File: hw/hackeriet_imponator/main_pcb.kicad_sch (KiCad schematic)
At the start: 10 parts, among them J1 AVR-ISP-6, J2 Battery connector, U1 ATmega328PB-A

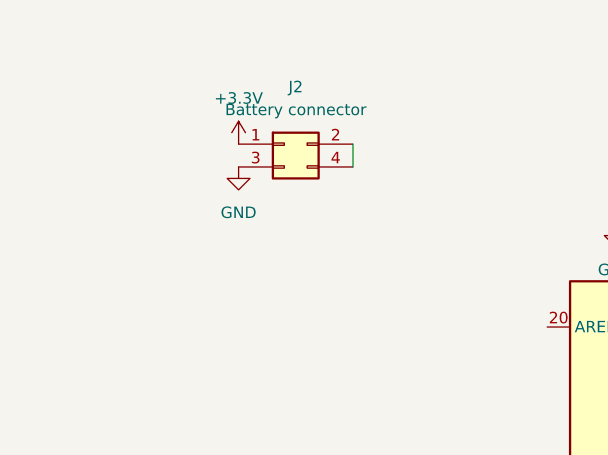
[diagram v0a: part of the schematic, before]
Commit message: Added Batttery holders. Some general routing
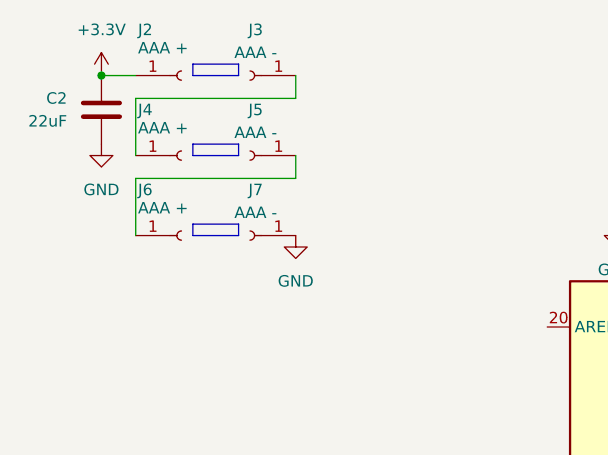
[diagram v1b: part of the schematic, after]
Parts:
- removed J2: Battery connector, imponator_footprint_lib:BAT_1022, symbol Connector_Generic:Conn_02x02_Odd_Even
- added C2: 22uF, Capacitor_SMD:C_0603_1608Metric_Pad1.08x0.95mm_HandSolder, symbol Device:C
- added J2, J4, J6: AAA +, imponator_footprint_lib:BAT_597, symbol Connector:Conn_01x01_Socket
- added J3, J5, J7: AAA -, imponator_footprint_lib:BAT_591, symbol Connector:Conn_01x01_Socket
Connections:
- net +3.3V: now also C2.2, J2.1 (Pin_1)
- net GND: now also C2.1, J7.1 (Pin_1)
- new net: J3.1 (Pin_1), J4.1 (Pin_1)
- new net: J5.1 (Pin_1), J6.1 (Pin_1)

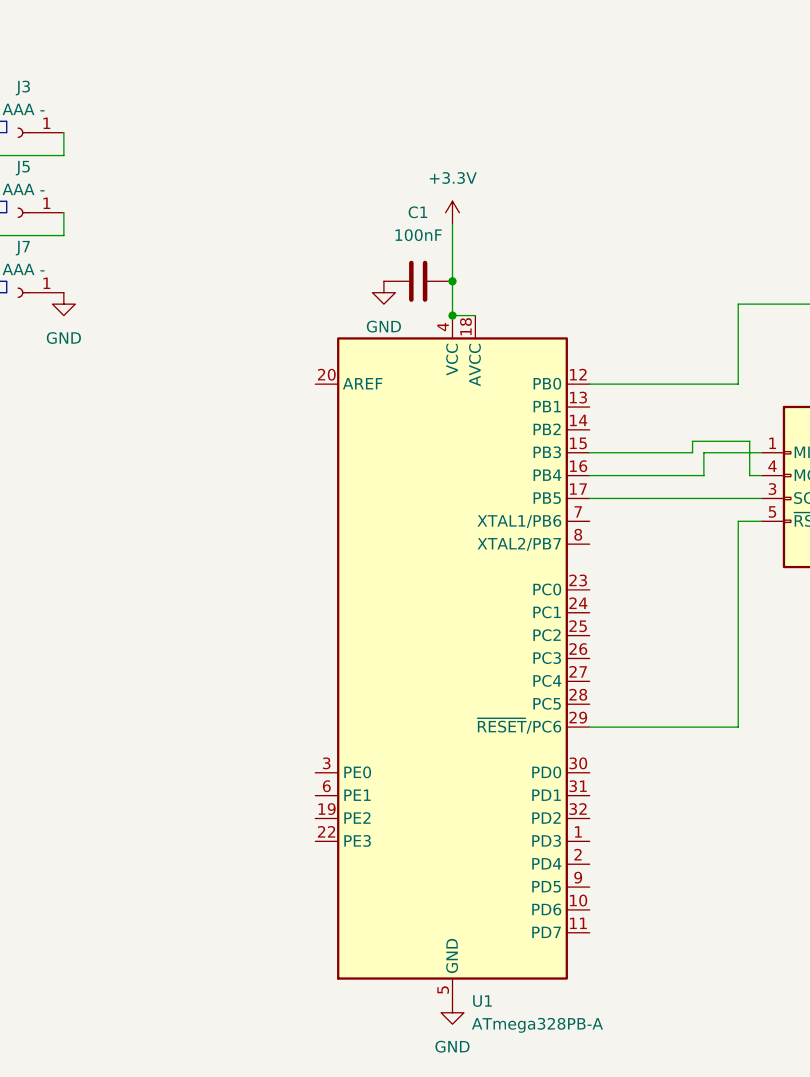
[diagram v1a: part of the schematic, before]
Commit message: Started changing out ATmega328P with ATmega32URC because the latter got built-in USB driver, making the design easier, if a bit more expensive
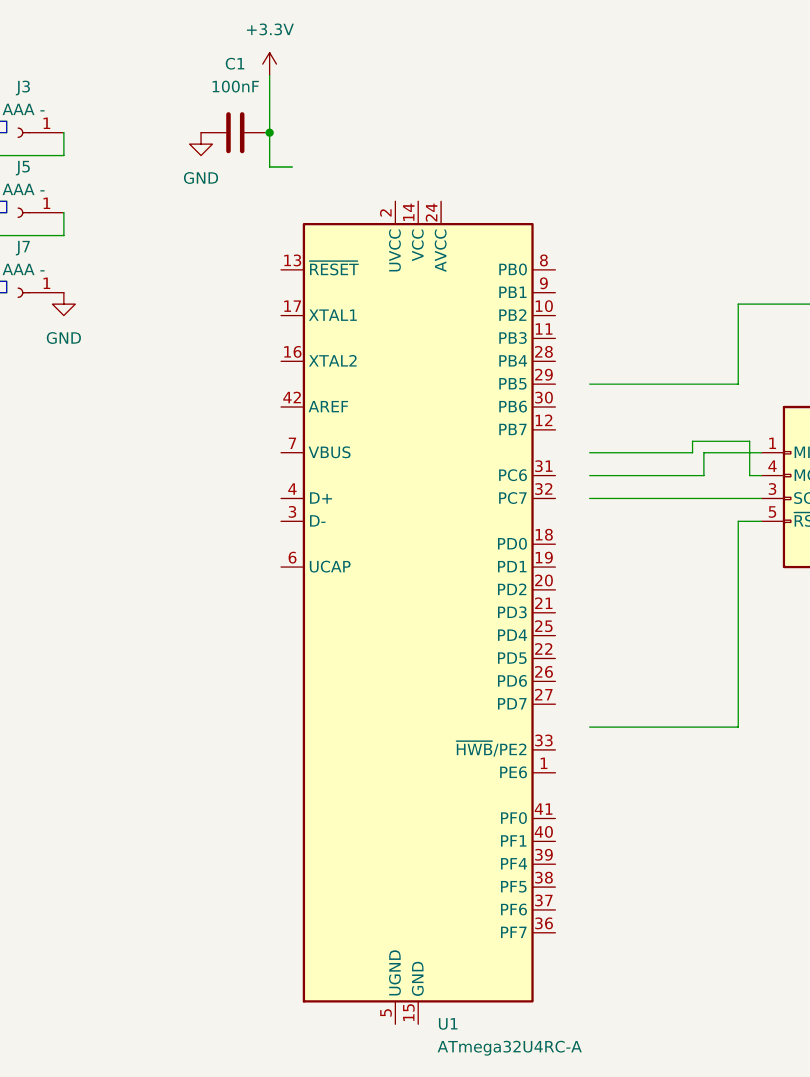
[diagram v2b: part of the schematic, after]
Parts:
- removed U1: ATmega328PB-A, Package_QFP:TQFP-32_7x7mm_P0.8mm, symbol MCU_Microchip_ATmega:ATmega328PB-A
- added U1: ATmega32U4RC-A, Package_QFP:TQFP-44_10x10mm_P0.8mm, symbol MCU_Microchip_ATmega:ATmega32U4RC-A
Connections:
- new net: U1.14 (VCC), U1.34 (VCC)
- new net: U1.15 (GND), U1.23 (GND), U1.35 (GND), U1.43 (GND)
- new net: U1.24 (AVCC), U1.44 (AVCC)
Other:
- moved on the sheet: C1

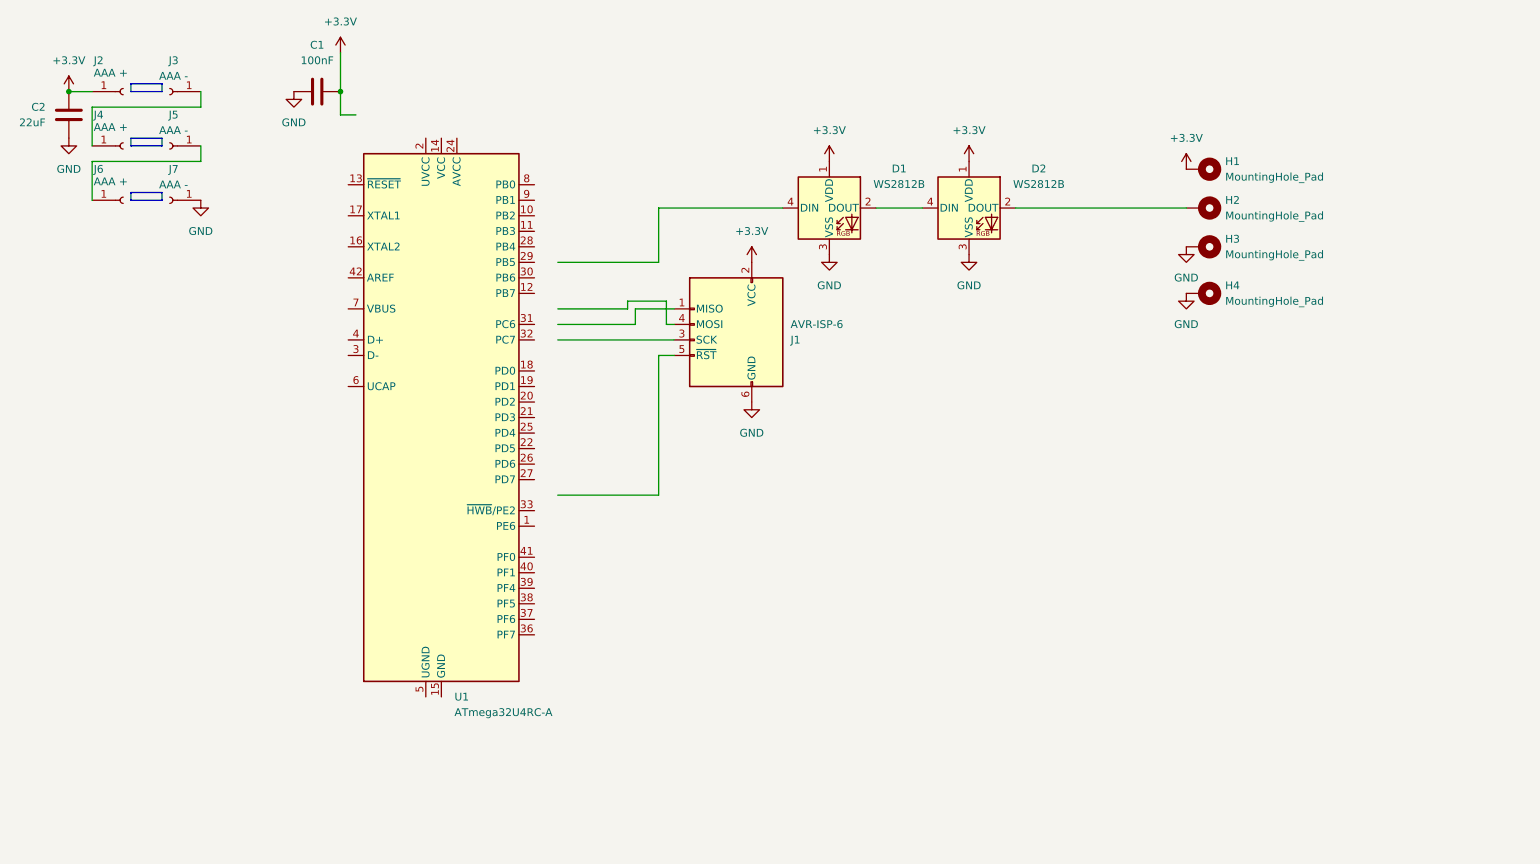
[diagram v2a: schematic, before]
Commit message: Major change. Resized PCB. Changed CPU. Added USB. Added headers. Added another layer for batteries
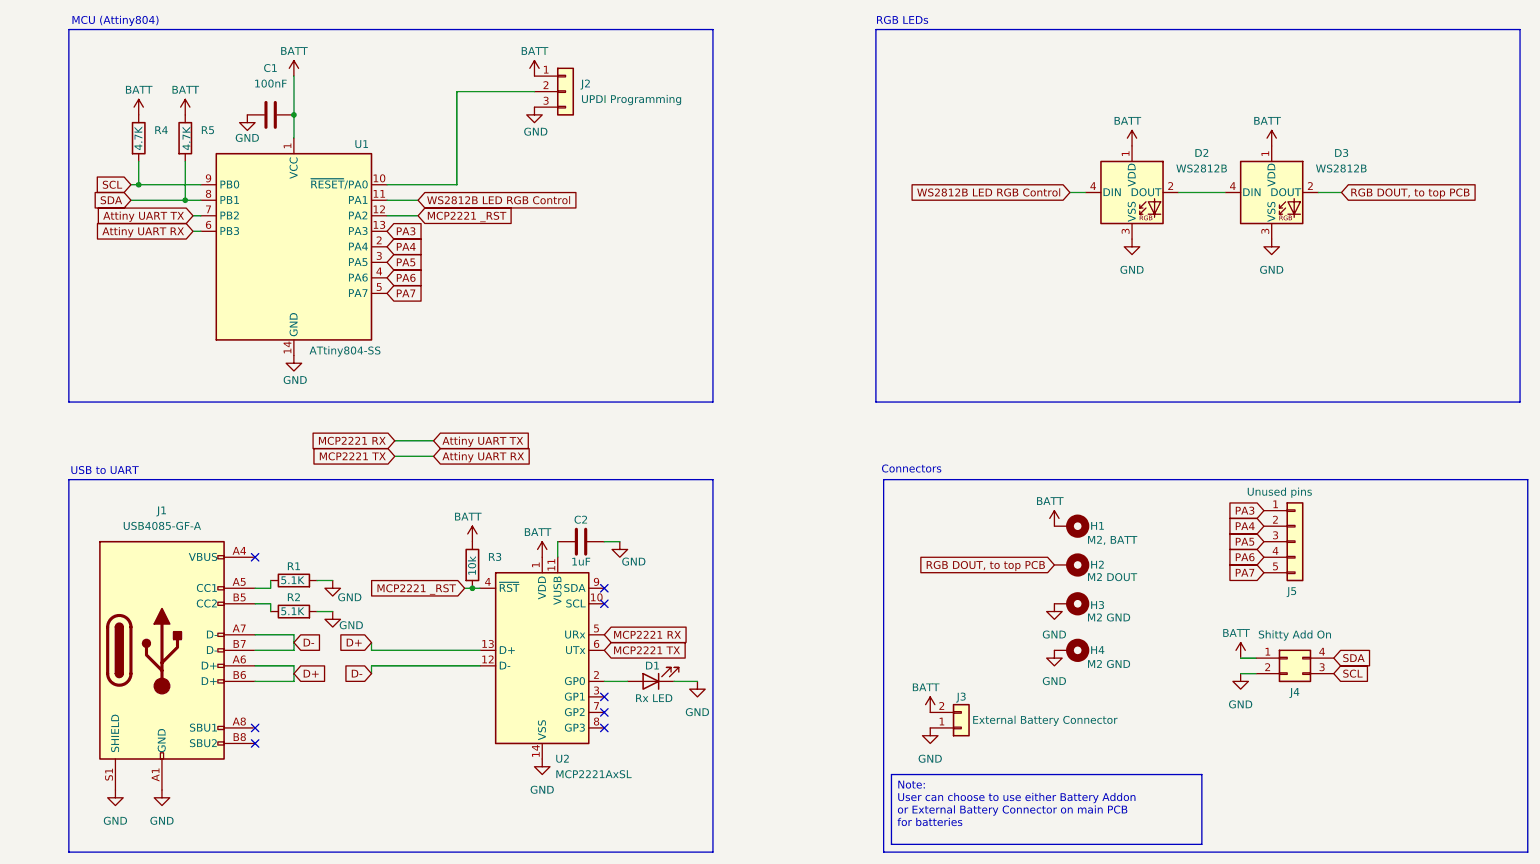
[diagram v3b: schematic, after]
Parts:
- removed J1: AVR-ISP-6, Connector_PinSocket_2.54mm:PinSocket_2x03_P2.54mm_Vertical_SMD, symbol Connector:AVR-ISP-6
- removed J2, J4, J6: AAA +, imponator_footprint_lib:BAT_597, symbol Connector:Conn_01x01_Socket
- removed J3, J5, J7: AAA -, imponator_footprint_lib:BAT_591, symbol Connector:Conn_01x01_Socket
- removed U1: ATmega32U4RC-A, Package_QFP:TQFP-44_10x10mm_P0.8mm, symbol MCU_Microchip_ATmega:ATmega32U4RC-A
- added D1: Rx LED, LED_SMD:LED_0603_1608Metric_Pad1.05x0.95mm_HandSolder, symbol Device:LED
- added J1: USB4085-GF-A, Connector_USB:USB_C_Receptacle_GCT_USB4085, symbol Connector:USB_C_Receptacle_USB2.0_16P
- added J2: UPDI Programming, Connector_PinHeader_2.54mm:PinHeader_1x03_P2.54mm_Horizontal, symbol Connector_Generic:Conn_01x03
- added J3: External Battery Connector, Connector_PinHeader_2.54mm:PinHeader_1x02_P2.54mm_Vertical, symbol Connector_Generic:Conn_01x02
- added J4: Shitty Add On, Connector_PinHeader_2.54mm:PinHeader_2x02_P2.54mm_Horizontal, symbol Connector_Generic:Conn_02x02_Counter_Clockwise
- added J5: Unused pins, Connector_PinSocket_2.54mm:PinSocket_1x05_P2.54mm_Vertical_SMD_Pin1Left, symbol Connector_Generic:Conn_01x05
- added R1, R2: 5.1K, Resistor_SMD:R_0603_1608Metric_Pad0.98x0.95mm_HandSolder, symbol Device:R
- added R3: 10k, Resistor_SMD:R_0603_1608Metric_Pad0.98x0.95mm_HandSolder, symbol Device:R
- added R4, R5: 4.7K, Resistor_SMD:R_0603_1608Metric_Pad0.98x0.95mm_HandSolder, symbol Device:R
- added U1: ATtiny804-SS, Package_SO:SOIC-14_3.9x8.7mm_P1.27mm, symbol MCU_Microchip_ATtiny:ATtiny804-SS
- added U2: MCP2221AxSL, Package_SO:SOIC-14_3.9x8.7mm_P1.27mm, symbol Interface_USB:MCP2221AxSL
- C2: value 22uF -> 1uF
- H1: value MountingHole_Pad -> M2, BATT; footprint MountingHole:MountingHole_3.2mm_M3_Pad_Via -> MountingHole:MountingHole_2.5mm_Pad_TopBottom
- H2: value MountingHole_Pad -> M2 DOUT; footprint MountingHole:MountingHole_3.2mm_M3_Pad_Via -> MountingHole:MountingHole_2.5mm_Pad_TopBottom
- H3, H4: value MountingHole_Pad -> M2 GND; footprint MountingHole:MountingHole_3.2mm_M3_Pad_Via -> MountingHole:MountingHole_2.5mm_Pad_TopBottom
- renumbered D1 to D2, D2 to D3
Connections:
- net GND: now also C2.2, D1.1 (K), J1.A1 (GND), J1.A12 (GND), J1.B1 (GND), J1.B12 (GND), J1.S1 (SHIELD), J2.3 (Pin_3), J3.1 (Pin_1), J4.2 (Pin_2), R1.2, R2.2, U1.14 (GND), U2.14 (VSS); no longer C2.1
- net WS2812B LED RGB Control: now reaches D2.4 (DIN)
- net WS2812B LED RGB Control: now also U1.11 (PA1)
- net RGB DOUT, to top PCB: now reaches D3.2 (DOUT), H2.1
- net +3.3V renamed BATT
- net BATT: now also J2.1 (Pin_1), J3.2 (Pin_2), J4.1 (Pin_1), R3.1, R4.1, R5.1, U1.1 (VCC), U2.1 (VDD); no longer C2.2
- new net: J1.A5 (CC1), R1.1
- new net: C2.1, U2.11 (VUSB)
- new net: J1.A4 (VBUS), J1.A9 (VBUS), J1.B4 (VBUS), J1.B9 (VBUS)
- new net: J1.B5 (CC2), R2.1
- new net: J2.2 (Pin_2), U1.10 (~{RESET}/PA0)
- new net: D1.2 (A), U2.2 (GP0)
- new net Attiny UART RX: U1.6 (PB3), U2.6 (UTx)
- new net Attiny UART TX: U1.7 (PB2), U2.5 (URx)
- new net D+: J1.A6 (D+), J1.B6 (D+), U2.13 (D+)
- new net D-: J1.A7 (D-), J1.B7 (D-), U2.12 (D-)
- new net MCP2221 _RST: R3.2, U1.12 (PA2), U2.4 (~{RST})
- new net PA3: J5.1 (Pin_1), U1.13 (PA3)
- new net PA4: J5.2 (Pin_2), U1.2 (PA4)
- new net PA5: J5.3 (Pin_3), U1.3 (PA5)
- new net PA6: J5.4 (Pin_4), U1.4 (PA6)
- new net PA7: J5.5 (Pin_5), U1.5 (PA7)
- new net SCL: J4.3 (Pin_3), R4.2, U1.9 (PB0)
- new net SDA: J4.4 (Pin_4), R5.2, U1.8 (PB1)
- no-connect marks 0 -> 8
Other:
- note added: "Connectors"
- note added: "MCU (Attiny804)"
- note added: "RGB LEDs"
- note added: "USB to UART"
- company: (none) -> Hackeriet
- title: (none) -> Imponator, Main PCB
- moved on the sheet: C1, D2, D3, H1, H2, H3, H4

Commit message: Removed outer ring and battery backplate. Ready to apply TODOs
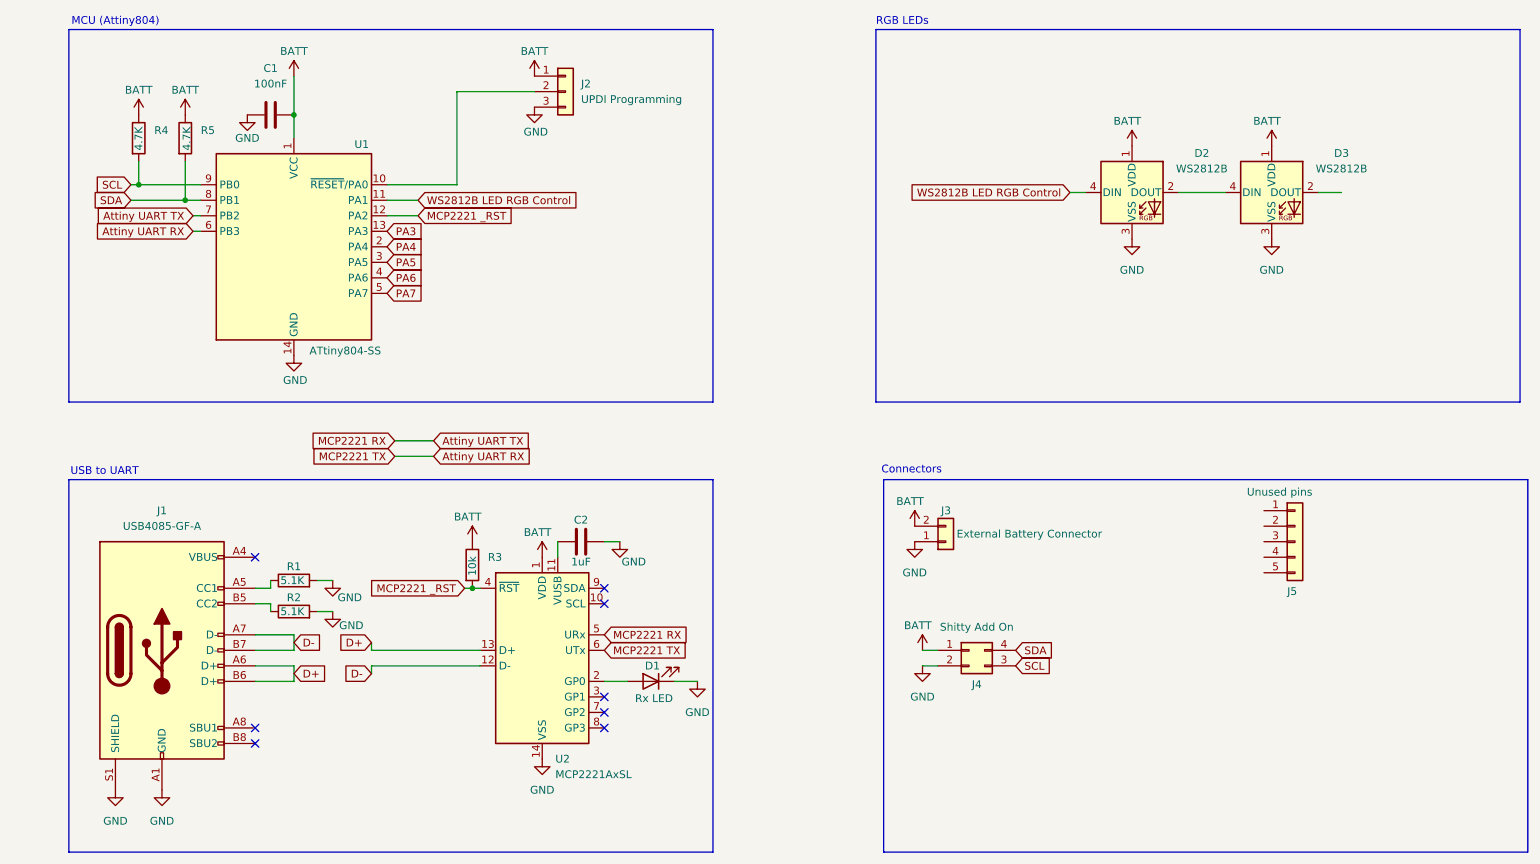
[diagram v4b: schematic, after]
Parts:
- removed H1: M2, BATT, MountingHole:MountingHole_2.5mm_Pad_TopBottom, symbol Mechanical:MountingHole_Pad
- removed H2: M2 DOUT, MountingHole:MountingHole_2.5mm_Pad_TopBottom, symbol Mechanical:MountingHole_Pad
- removed H3, H4: M2 GND, MountingHole:MountingHole_2.5mm_Pad_TopBottom, symbol Mechanical:MountingHole_Pad
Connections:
- net PA3: no longer J5.1 (Pin_1)
- net PA4: no longer J5.2 (Pin_2)
- net PA5: no longer J5.3 (Pin_3)
- net PA6: no longer J5.4 (Pin_4)
- net PA7: no longer J5.5 (Pin_5)
- net RGB DOUT, to top PCB: no longer names the net of D3.2 (DOUT)
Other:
- moved on the sheet: J3, J4
